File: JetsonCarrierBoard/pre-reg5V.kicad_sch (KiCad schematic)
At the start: 20 parts

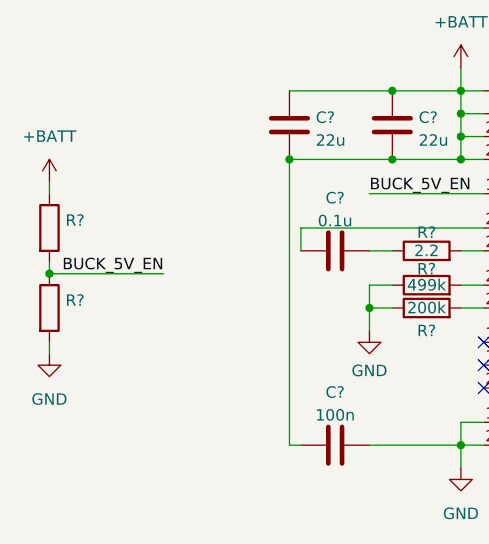
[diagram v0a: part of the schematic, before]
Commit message: Fan and Debug UART
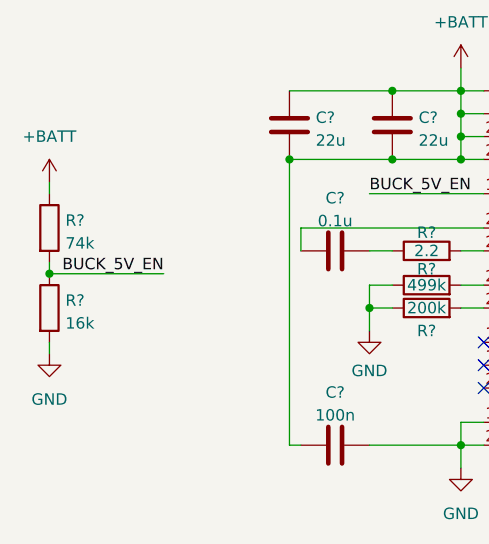
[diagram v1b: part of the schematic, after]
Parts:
- R?: value (none) -> 74k
- R?: value (none) -> 16k
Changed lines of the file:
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@@
       (effects (font (size 1.27 1.27)) (justify left))
     )
-    (property "Value" "" (id 1) (at 86.868 98.2222 0)
+    (property "Value" "74k" (id 1) (at 86.868 98.2222 0)
       (effects (font (size 1.27 1.27)) (justify left))
     )
@@
       (effects (font (size 1.27 1.27)) (justify left))
     )
-    (property "Value" "" (id 1) (at 86.868 107.1122 0)
+    (property "Value" "16k" (id 1) (at 86.868 107.1122 0)
       (effects (font (size 1.27 1.27)) (justify left))
     )

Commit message: Adding more Title block info and changing main hierarchical page layout
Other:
- title: (none) -> Pre-Reg 5V
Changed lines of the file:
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@@
 (kicad_sch (version 20211123) (generator eeschema)
   (paper "A4")
+  (title_block
+    (title "Pre-Reg 5V")
+    (date "2022-09-18")
+    (rev "1.0")
+  )
   (junction (at 171.45 96.52) (diameter 0) (color 0 0 0 0)
   )
